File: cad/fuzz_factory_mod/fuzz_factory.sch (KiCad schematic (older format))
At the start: 26 parts

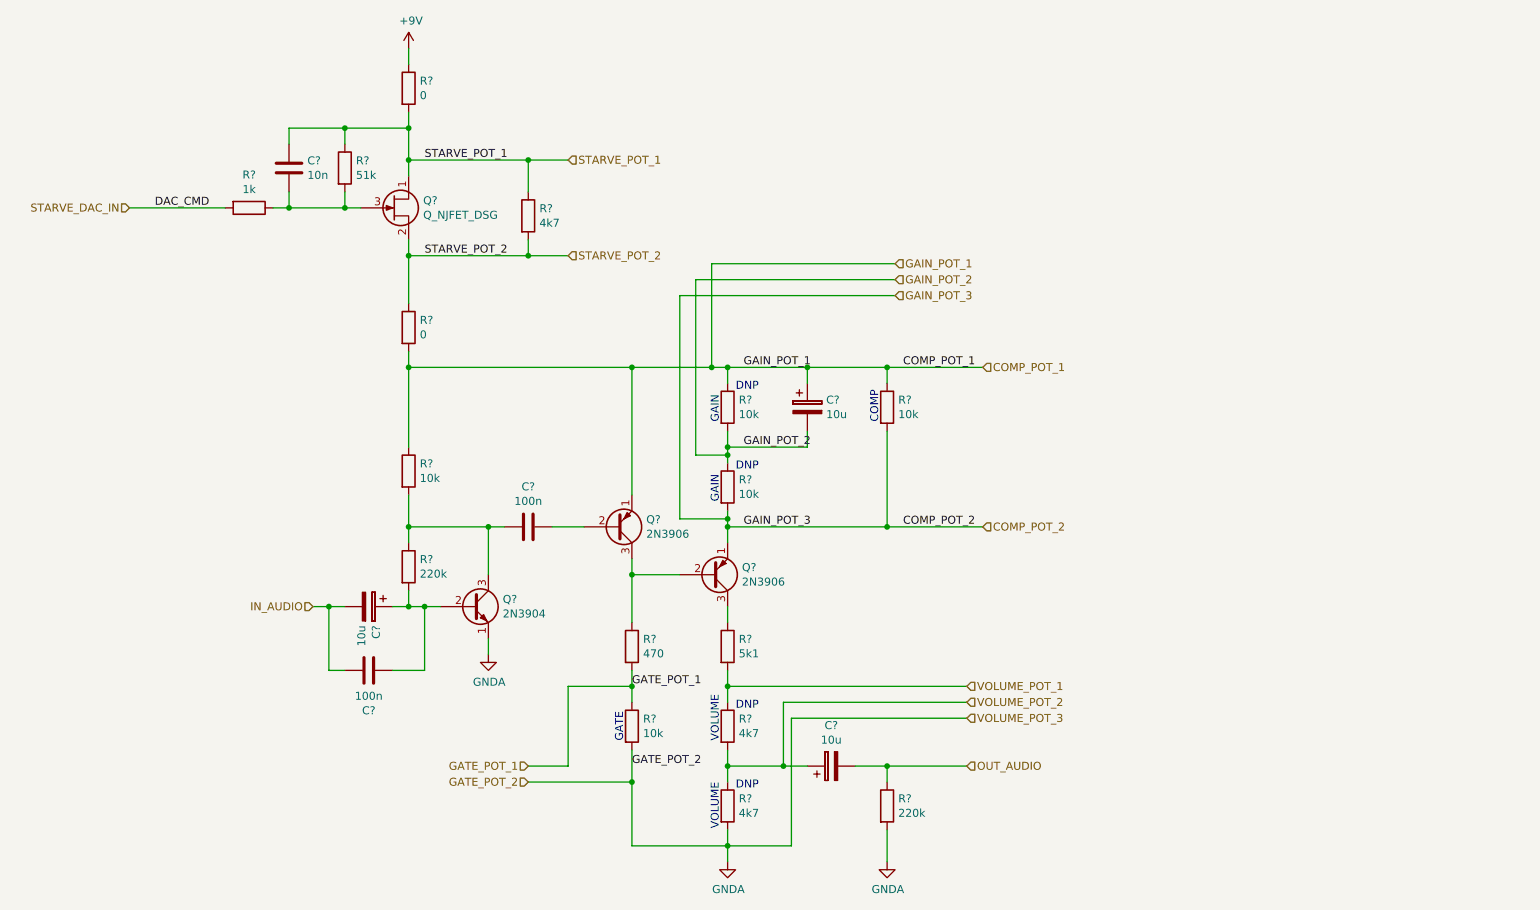
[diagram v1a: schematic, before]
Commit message: Continued schematic.
Modified fuuz_factory circuit : use of matched transistor pairs.
Added USB interface, through FT230X and direct to MCU.
Associated footprints, except for XTAL and trimmers.
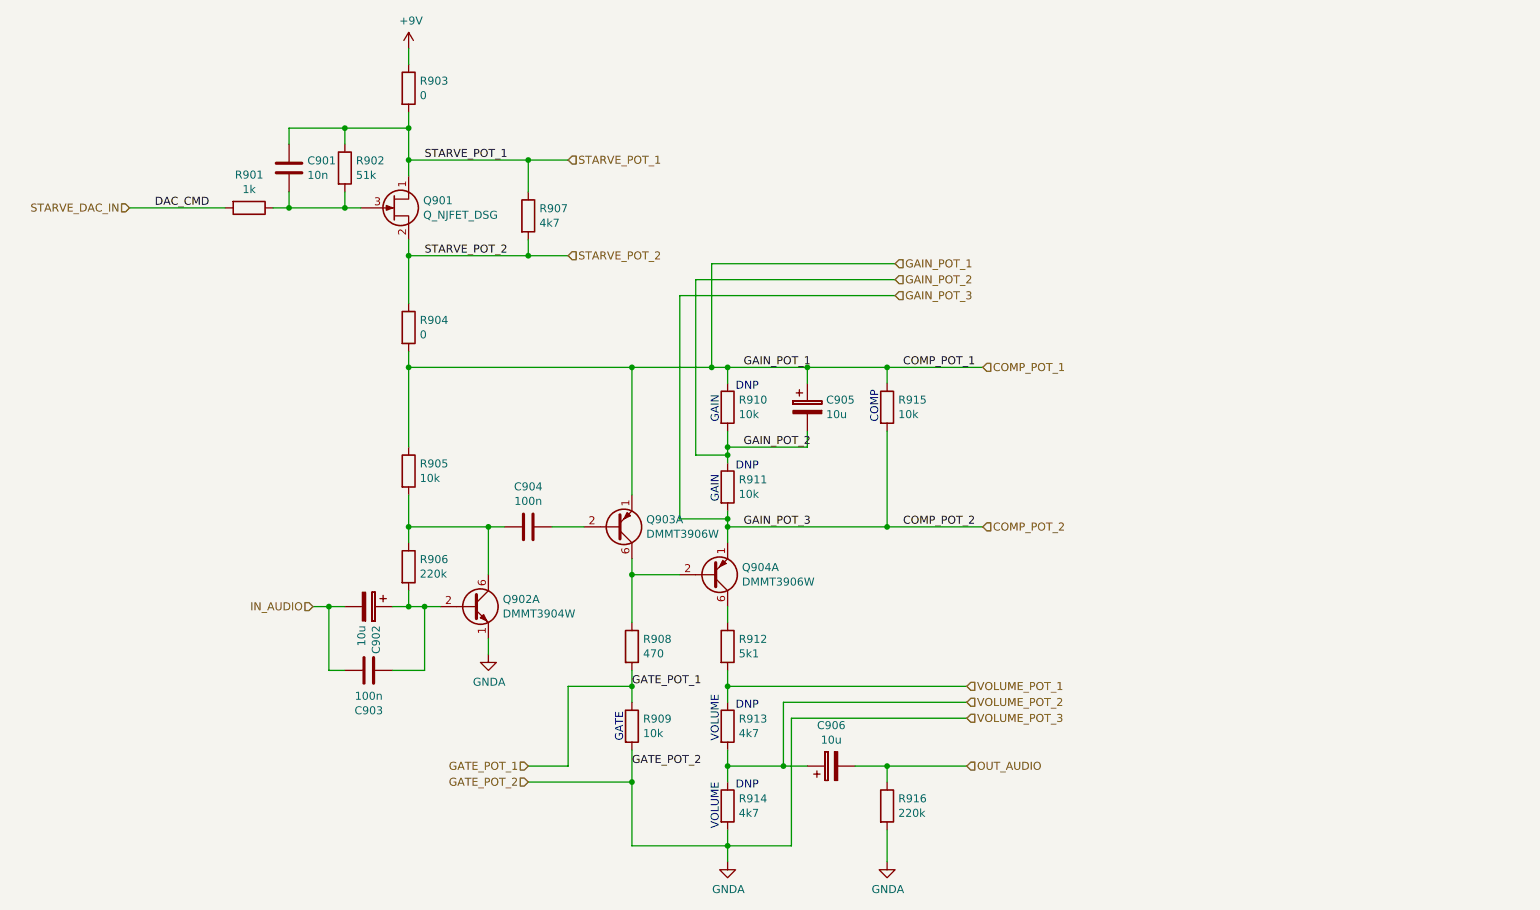
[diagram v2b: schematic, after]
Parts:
- removed Q?: 2N3904, Package_TO_SOT_THT:TO-92_Inline, symbol Transistor_BJT:2N3904
- removed Q? (x2): 2N3906, Package_TO_SOT_THT:TO-92_Inline, symbol Transistor_BJT:2N3906
- added Q902: DMMT3904W, Package_TO_SOT_SMD:SOT-363_SC-70-6, symbol Transistor_BJT:BC846BDW1
- added Q903, Q904: DMMT3906W, Package_TO_SOT_SMD:SOT-363_SC-70-6, symbol Transistor_BJT:BC857BDW1
- C901, C903, C904: renamed from C?; footprint (none) -> Capacitors_SMD:C_0603
- C902, C905, C906: renamed from C?; footprint (none) -> Capacitors_SMD:CP_Elec_6.3x4.5
- Q901: renamed from Q?; footprint (none) -> TO_SOT_Packages_SMD:SOT-23
- R901, R902, R903, R904, R905, R906, R907, R908, R909, R910, R911, R912, R913, R914, R915, R916: renamed from R?; footprint (none) -> Resistors_SMD:R_0603
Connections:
- net COMP_POT_1: now also Q903.1 (E1)
- net COMP_POT_2: now also Q904.1 (E1)
- net GNDA: now also Q902.1 (E1)
- net at C904.2, R905.2, R906.1: now also Q902.6 (C1)
- net at C902.1, C903.2, R906.2: now also Q902.2 (B1)
- net at C904.1: now also Q903.2 (B1)
- net at R908.1: now also Q903.6 (C1), Q904.2 (B1)
- net at R912.1: now also Q904.6 (C1)

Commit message: Continued schematic.
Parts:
- Q902, Q903, Q904: footprint Package_TO_SOT_SMD:SOT-363_SC-70-6 -> TO_SOT_Packages_SMD:SOT-363_SC-70-6
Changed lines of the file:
@@
 $Descr A4 11693 8268
 encoding utf-8
-Sheet 9 22
+Sheet 9 26
 Title ""
 Date ""
@@
 F 0 "Q903" H 5240 3954 50  0000 L CNN
 F 1 "DMMT3906W" H 5240 4045 50  0000 L CNN
-F 2 "Package_TO_SOT_SMD:SOT-363_SC-70-6" H 5250 4100 50  0001 C CNN
+F 2 "TO_SOT_Packages_SMD:SOT-363_SC-70-6" H 5250 4100 50  0001 C CNN
 F 3 "http://www.onsemi.com/pub_link/Collateral/BC856BDW1T1-D.PDF" H 5050 4000 50  0001 C CNN
 	1    5050 4000
@@
 F 0 "Q904" H 5840 4254 50  0000 L CNN
 F 1 "DMMT3906W" H 5840 4345 50  0000 L CNN
-F 2 "Package_TO_SOT_SMD:SOT-363_SC-70-6" H 5850 4400 50  0001 C CNN
+F 2 "TO_SOT_Packages_SMD:SOT-363_SC-70-6" H 5850 4400 50  0001 C CNN
 F 3 "http://www.onsemi.com/pub_link/Collateral/BC856BDW1T1-D.PDF" H 5650 4300 50  0001 C CNN
 	1    5650 4300
@@
 F 0 "Q902" H 4340 4546 50  0000 L CNN
 F 1 "DMMT3904W" H 4340 4455 50  0000 L CNN
-F 2 "Package_TO_SOT_SMD:SOT-363_SC-70-6" H 4350 4600 50  0001 C CNN
+F 2 "TO_SOT_Packages_SMD:SOT-363_SC-70-6" H 4350 4600 50  0001 C CNN
 F 3 "http://www.onsemi.com/pub_link/Collateral/BC846BDW1T1-D.PDF" H 4150 4500 50  0001 C CNN
 	1    4150 4500
 	1    0    0    -1
 $EndComp
+$Sheet
+S 8900 1000 1100 250
+U 5EEB4E87
+F0 "ADC_frontend_1" 50
+F1 "ADC_frontend.sch" 50
+F2 "AN_IN_1" I L 8900 1050 50
+F3 "AN_MCU_1" I R 10000 1050 50
+F4 "AN_IN_2" I L 8900 1150 50
+F5 "AN_MCU_2" I R 10000 1150 50
+$EndSheet
 $EndSCHEMATC

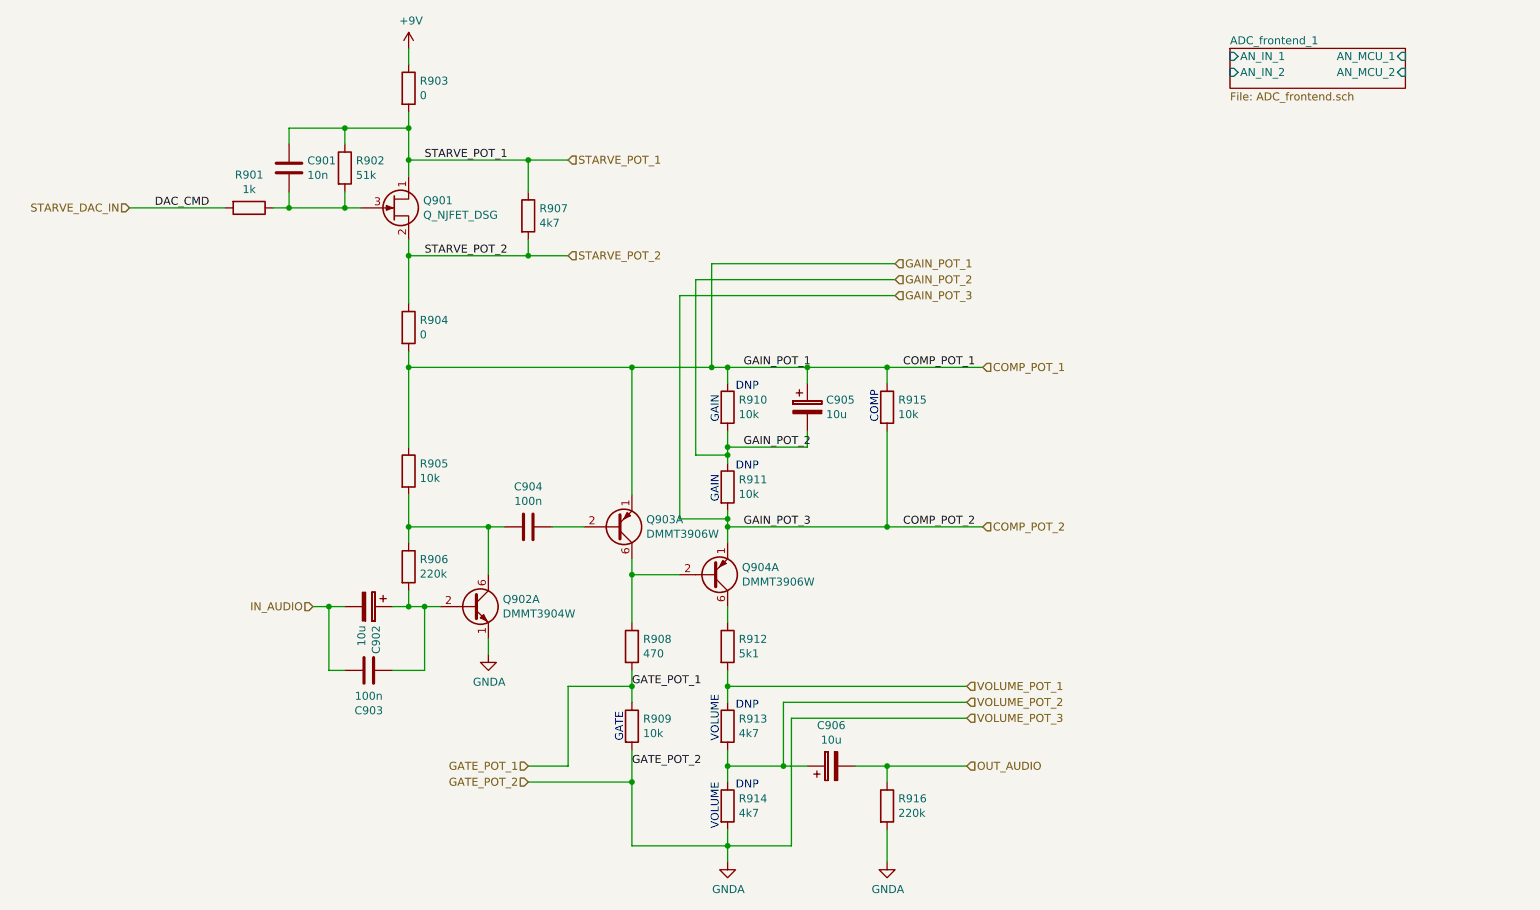
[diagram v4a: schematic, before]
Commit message: Continued schematic.
Continued component placement.
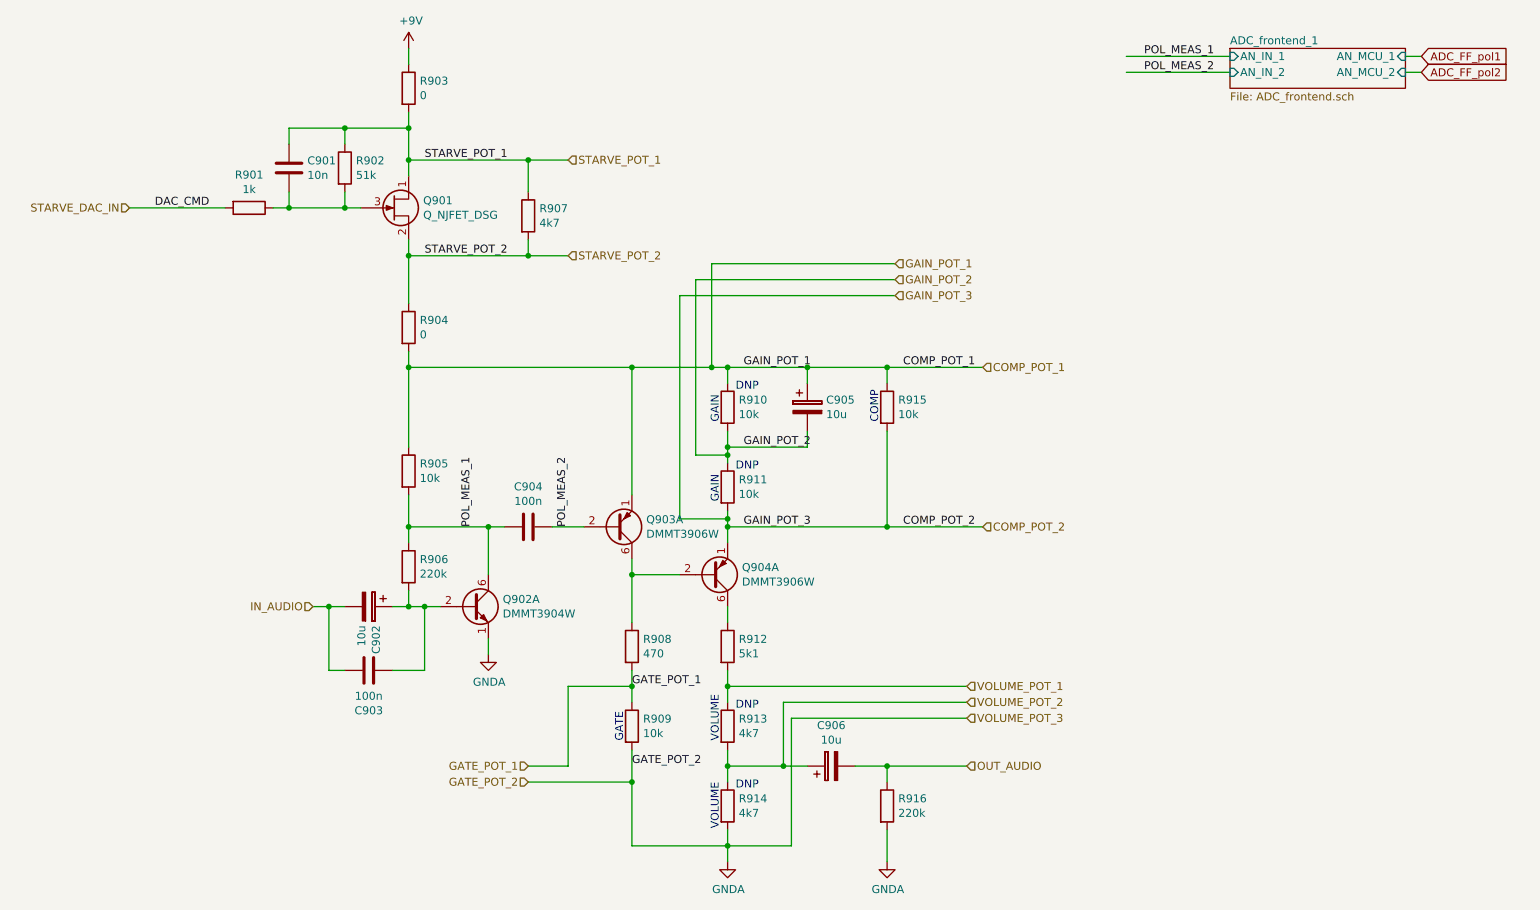
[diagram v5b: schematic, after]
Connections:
- net POL_MEAS_1: now reaches C904.2, Q902.6 (C1), R905.2, R906.1
- net POL_MEAS_2: now reaches C904.1, Q903.2 (B1)
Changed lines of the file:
@@
 $Descr A4 11693 8268
 encoding utf-8
-Sheet 9 30
+Sheet 17 30
 Title ""
 Date ""
@@
 F5 "AN_MCU_2" I R 10000 1150 50
 $EndSheet
+Text GLabel 10100 1050 2    50   Input ~ 0
+ADC_FF_pol1
+Text GLabel 10100 1150 2    50   Input ~ 0
+ADC_FF_pol2
+Wire Wire Line
+	10000 1050 10100 1050
+Wire Wire Line
+	10100 1150 10000 1150
+Text Label 4150 4000 1    50   ~ 0
+POL_MEAS_1
+Text Label 8800 1050 2    50   ~ 0
+POL_MEAS_1
+Wire Wire Line
+	8900 1050 8250 1050
+Text Label 4750 4000 1    50   ~ 0
+POL_MEAS_2
+Text Label 8800 1150 2    50   ~ 0
+POL_MEAS_2
+Wire Wire Line
+	8900 1150 8250 1150
 $EndSCHEMATC
